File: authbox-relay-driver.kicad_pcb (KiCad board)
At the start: 2 copper layers, 65 x 56 mm, 33 parts, among them J1 GPIO, J2 Screw_Terminal_01x12, Q1 2V7002L, Q2 BC846, Q3 BC846, Q4 2V7002L, U2 MCP1415

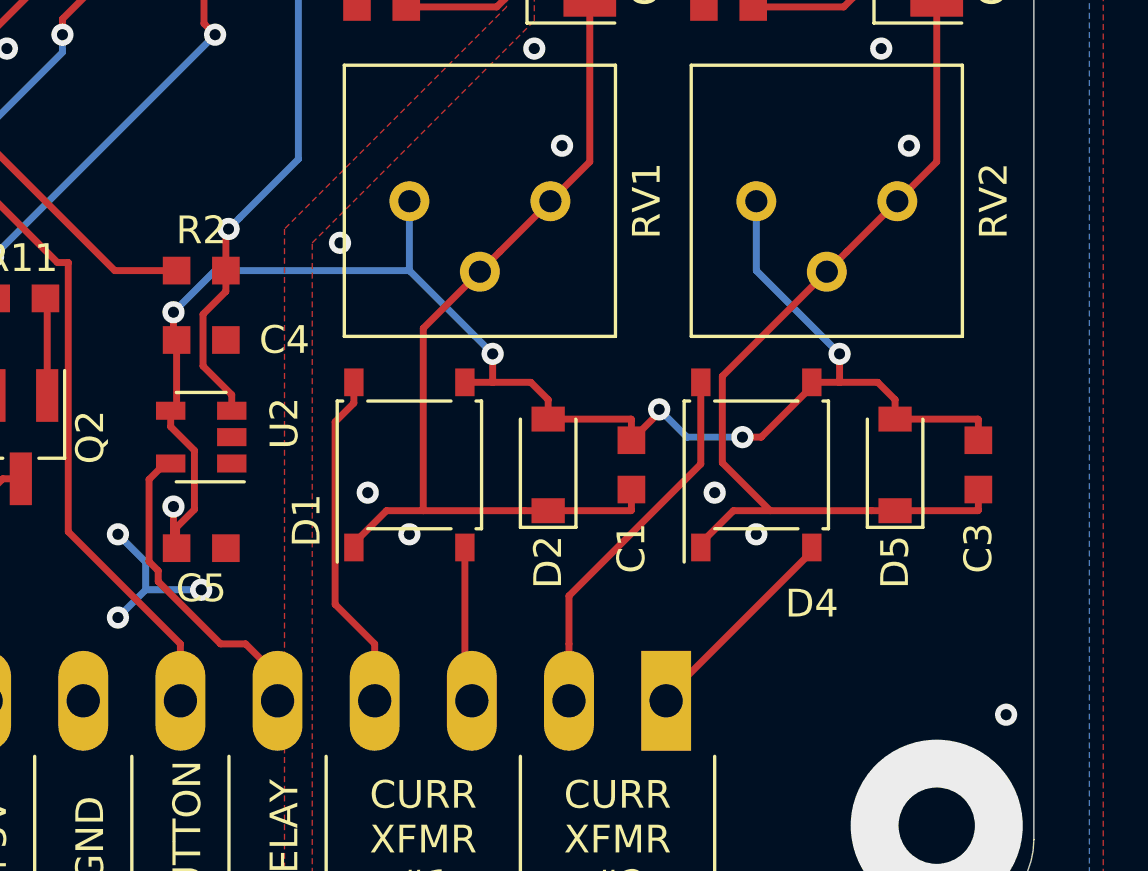
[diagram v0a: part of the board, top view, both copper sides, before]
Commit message: Fixed: * Rectifier bridge footprint. * Pad size for trimmer potentiometers.
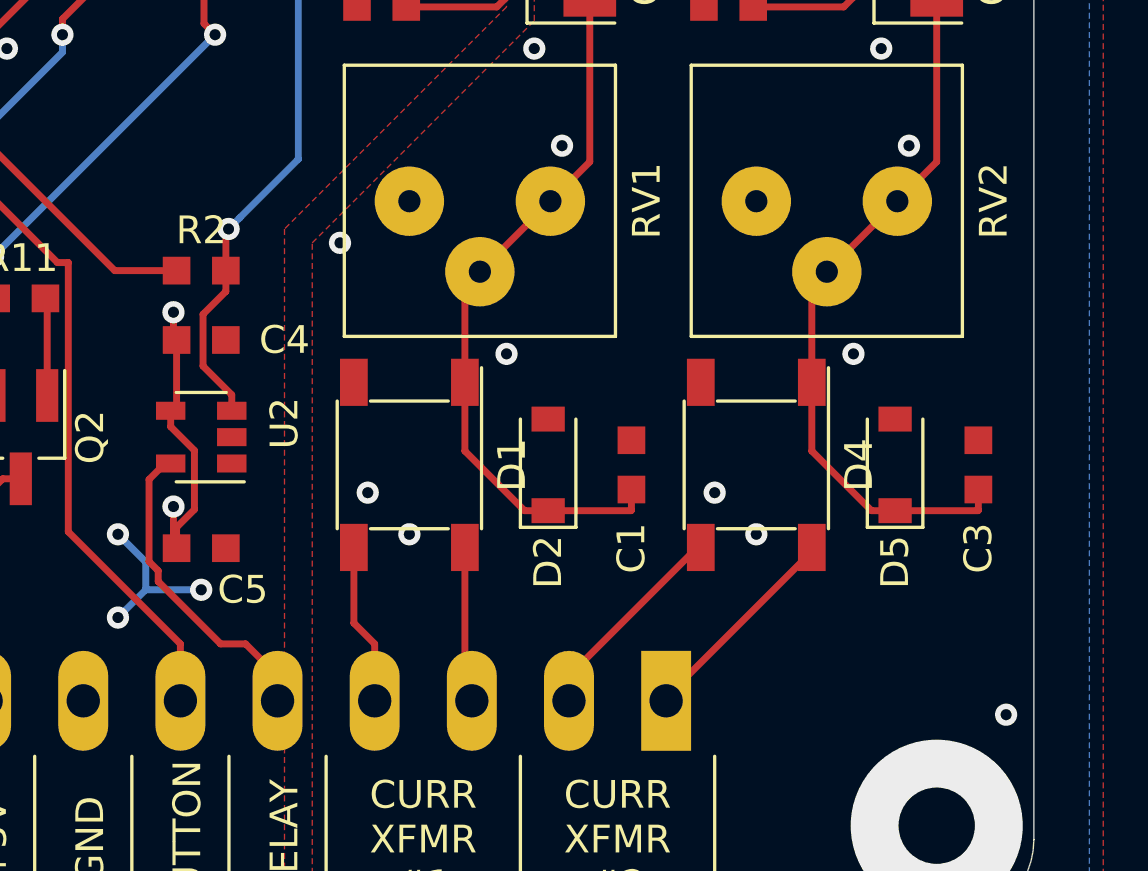
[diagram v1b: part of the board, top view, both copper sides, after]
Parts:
- turned D1 to 270 degrees
- turned D4 to 270 degrees
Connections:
- D1 pad 2: /current-sense/CURR_B -> GND
- D1 pad 3: GND -> /current-sense/CURR_A
- D1 pad 4: /current-sense/CURR_A -> /current-sense/CURR_B
- D4 pad 2: /sheet5C9BD5B1/CURR_B -> GND
- D4 pad 3: GND -> /sheet5C9BD5B1/CURR_A
- D4 pad 4: /sheet5C9BD5B1/CURR_A -> /sheet5C9BD5B1/CURR_B
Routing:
- net GND: track 146.0 -> 97.5 mm, vias 25 -> 23
- net Net-(C3-Pad1): track 33.5 -> 25.6 mm
- net Net-(C1-Pad1): track 32.1 -> 25.6 mm
- net /current-sense/CURR_A: track 12.3 -> 5.84 mm
- net /sheet5C9BD5B1/CURR_A: track 13.4 -> 7.57 mm

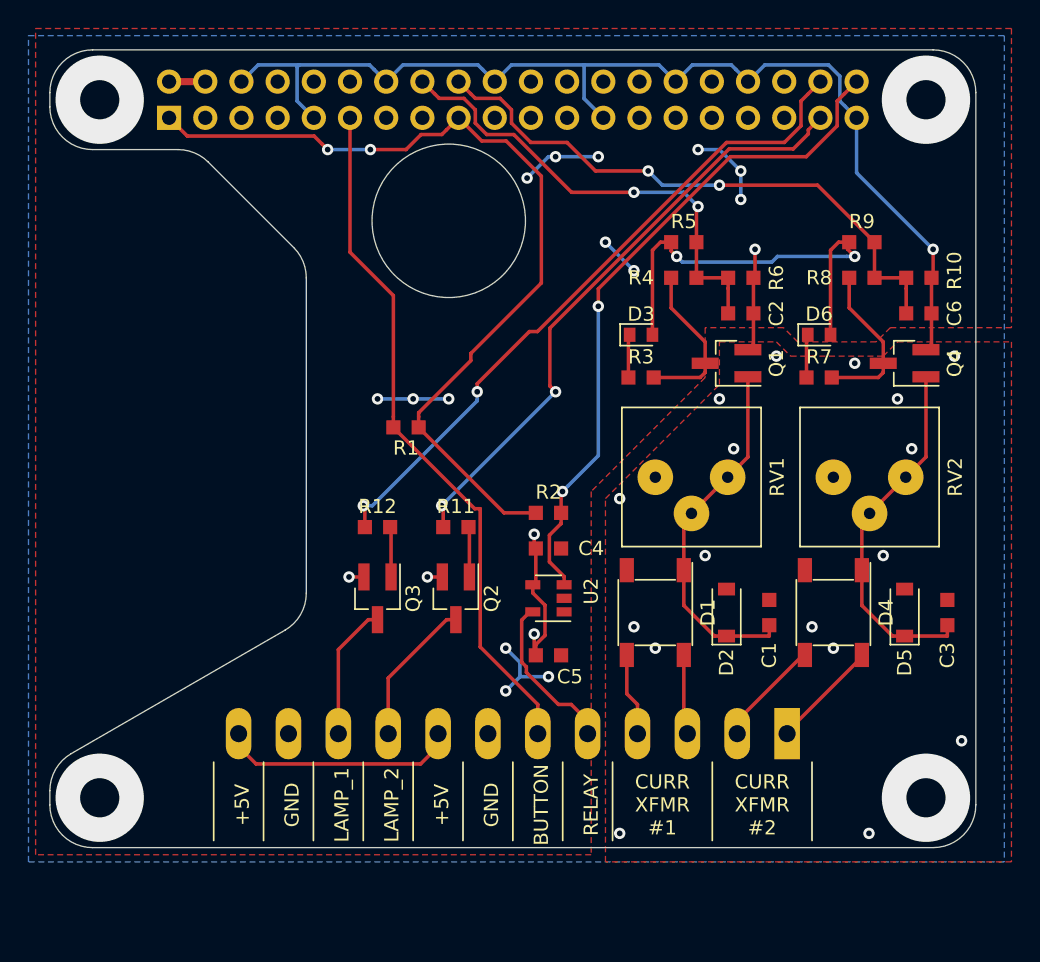
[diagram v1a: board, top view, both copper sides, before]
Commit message: Fixed a few solderability issues. Corrected the footprint for the rectifier bridges (D1 and D4).
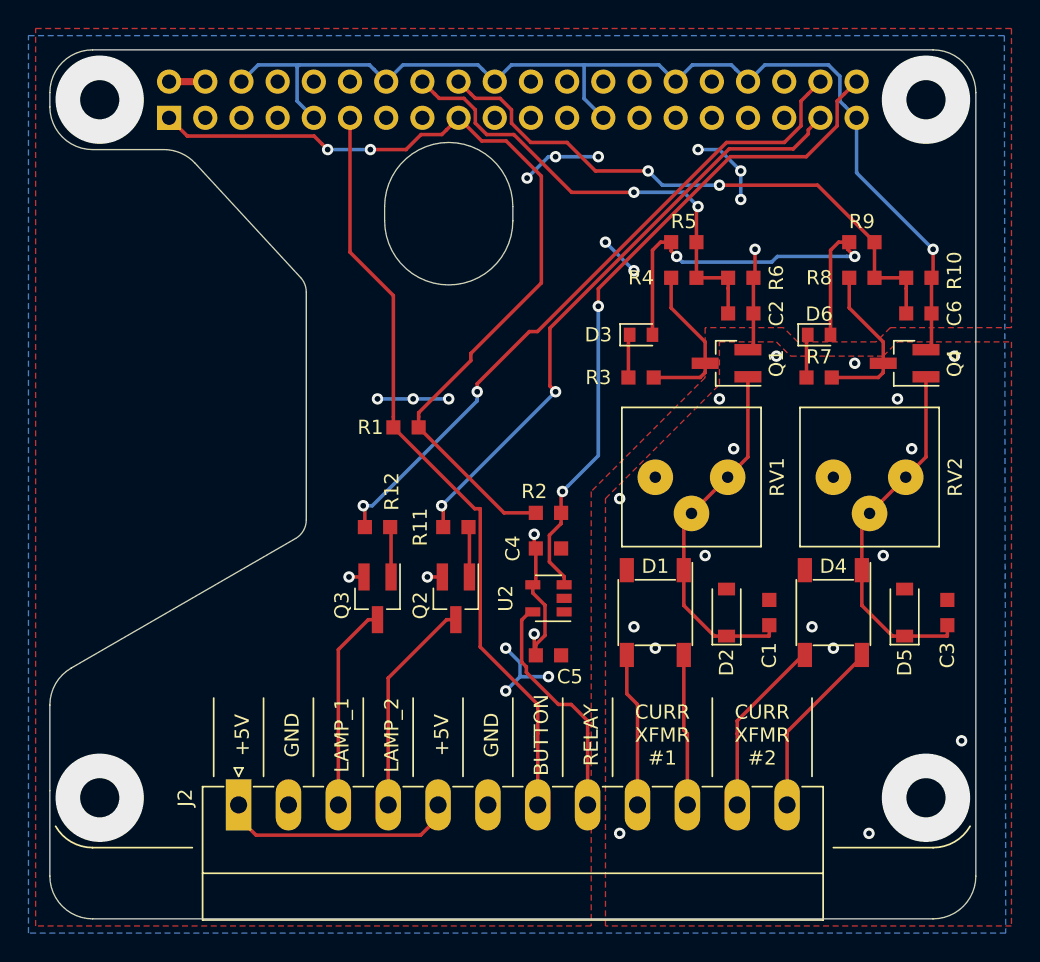
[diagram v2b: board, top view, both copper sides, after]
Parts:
- J2: moved to F.Cu
- moved J2 38.8 mm to (126.8, 139.7), turned to 0 degrees
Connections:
- J2 pad 1: /sheet5C9BD5B1/CURR_B -> +5V
- J2 pad 10: LAMP1 -> /current-sense/CURR_B
- J2 pad 11: GND -> /sheet5C9BD5B1/CURR_A
- J2 pad 12: +5V -> /sheet5C9BD5B1/CURR_B
- J2 pad 2: /sheet5C9BD5B1/CURR_A -> GND
- J2 pad 3: /current-sense/CURR_B -> LAMP1
- J2 pad 4: /current-sense/CURR_A -> LAMP2
- J2 pad 5: Net-(J2-Pad5) -> +5V
- J2 pad 6: B1_LOGIC -> GND
- J2 pad 7: GND -> B1_LOGIC
- J2 pad 8: +5V -> Net-(J2-Pad8)
- J2 pad 9: LAMP2 -> /current-sense/CURR_A
- U2 pad 5: Net-(J2-Pad5) -> Net-(J2-Pad8)
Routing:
- net Net-(J2-Pad8): track 0.00 -> 16.4 mm
- net Net-(J2-Pad5): track 11.4 -> 0.00 mm
- net LAMP2: track 10.3 -> 15.3 mm
- net LAMP1: track 9.52 -> 14.5 mm
- net B1_LOGIC: track 48.9 -> 53.9 mm
- net /current-sense/CURR_A: track 5.84 -> 10.8 mm
- net /sheet5C9BD5B1/CURR_B: track 7.70 -> 12.7 mm
- net /sheet5C9BD5B1/CURR_A: track 7.57 -> 12.6 mm
- net /current-sense/CURR_B: track 5.63 -> 10.6 mm
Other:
- board size 65 x 56 mm -> 65 x 61 mm

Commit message: Replace out of stock 2V7002 with 2N7002. Upgrade to KiCad 7.0.
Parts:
- C1, C3: value C -> 1µF
- C4, C5: value C -> 100nF
- Q1, Q4: value 2V7002L -> 2N7002L
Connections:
- C1 pad 1: Net-(C1-Pad1) -> Net-(D1-+)
- C3 pad 1: Net-(C3-Pad1) -> Net-(D4-+)
- D1 pad 1: Net-(C1-Pad1) -> Net-(D1-+)
- D2 pad 1: Net-(C1-Pad1) -> Net-(D1-+)
- D4 pad 1: Net-(C3-Pad1) -> Net-(D4-+)
- D5 pad 1: Net-(C3-Pad1) -> Net-(D4-+)
- J1 pad 10: Net-(J1-Pad10) -> unconnected-(J1-Pin_10-Pad10)
- J1 pad 12: Net-(J1-Pad12) -> unconnected-(J1-Pin_12-Pad12)
- J1 pad 13: Net-(J1-Pad13) -> unconnected-(J1-Pin_13-Pad13)
- J1 pad 15: Net-(J1-Pad15) -> unconnected-(J1-Pin_15-Pad15)
- J1 pad 19: Net-(J1-Pad19) -> unconnected-(J1-Pin_19-Pad19)
- J1 pad 21: Net-(J1-Pad21) -> unconnected-(J1-Pin_21-Pad21)
- J1 pad 22: Net-(J1-Pad22) -> unconnected-(J1-Pin_22-Pad22)
- J1 pad 23: Net-(J1-Pad23) -> unconnected-(J1-Pin_23-Pad23)
- J1 pad 24: Net-(J1-Pad24) -> unconnected-(J1-Pin_24-Pad24)
- J1 pad 26: Net-(J1-Pad26) -> unconnected-(J1-Pin_26-Pad26)
- J1 pad 27: Net-(J1-Pad27) -> unconnected-(J1-Pin_27-Pad27)
- J1 pad 28: Net-(J1-Pad28) -> unconnected-(J1-Pin_28-Pad28)
- J1 pad 29: Net-(J1-Pad29) -> unconnected-(J1-Pin_29-Pad29)
- J1 pad 3: Net-(J1-Pad3) -> unconnected-(J1-Pin_3-Pad3)
- J1 pad 31: Net-(J1-Pad31) -> unconnected-(J1-Pin_31-Pad31)
- J1 pad 32: Net-(J1-Pad32) -> unconnected-(J1-Pin_32-Pad32)
- J1 pad 33: Net-(J1-Pad33) -> unconnected-(J1-Pin_33-Pad33)
- J1 pad 35: Net-(J1-Pad35) -> unconnected-(J1-Pin_35-Pad35)
- J1 pad 36: Net-(J1-Pad36) -> unconnected-(J1-Pin_36-Pad36)
- J1 pad 5: Net-(J1-Pad5) -> unconnected-(J1-Pin_5-Pad5)
- J1 pad 7: Net-(J1-Pad7) -> unconnected-(J1-Pin_7-Pad7)
- J1 pad 8: Net-(J1-Pad8) -> unconnected-(J1-Pin_8-Pad8)
- Q1 pad 1: Net-(C1-Pad1) -> Net-(D1-+)
- Q4 pad 1: Net-(C3-Pad1) -> Net-(D4-+)
- U2 pad 1: Net-(U2-Pad1) -> unconnected-(U2-NC-Pad1)
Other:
- net class Default removed

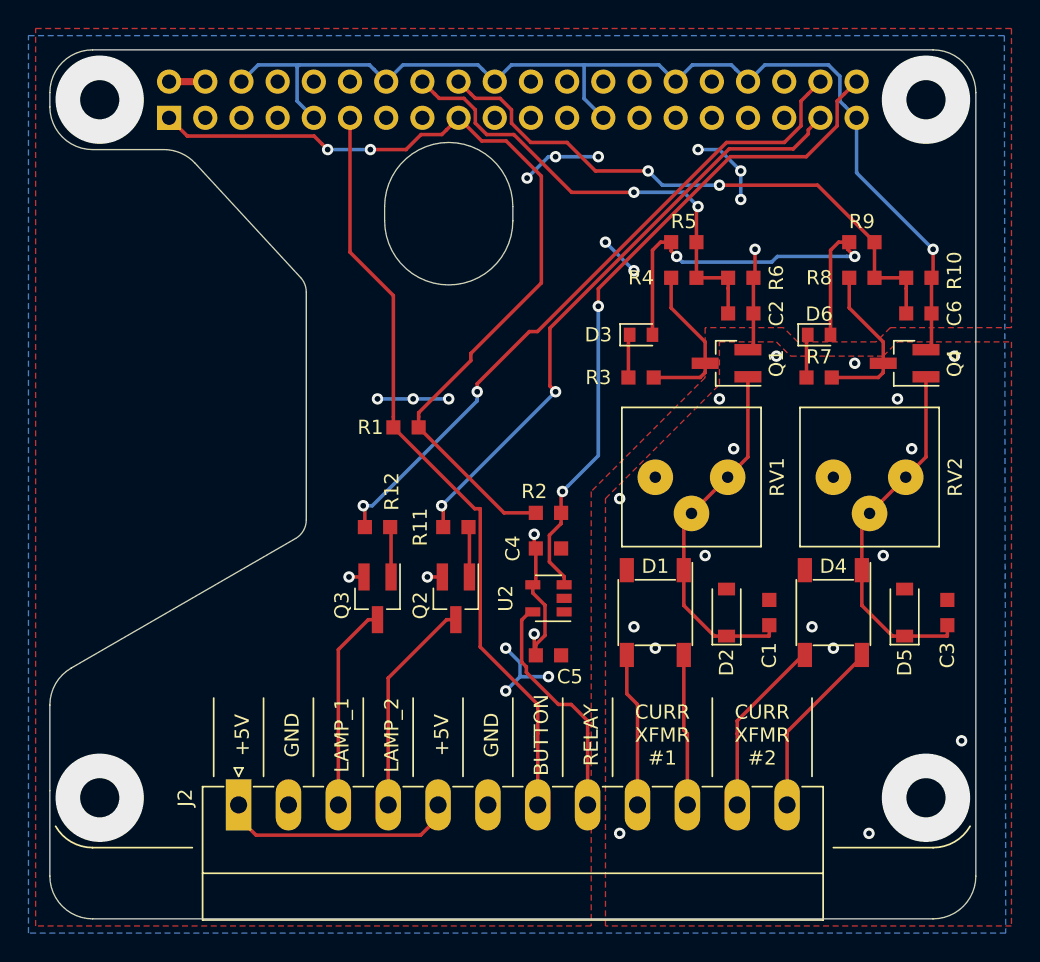
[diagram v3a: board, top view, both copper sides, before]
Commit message: Miscellaneous fixes: * Change to KiCad 8.0. * Modify the cutouts on the board to accomodate a different layout of the   PoE hat (which sits below.) * Transfer the customized footprints into a project-specific "hat-library"   footprints library, rather than leave them with local edits. * Change the mounting holes from through-plated to NPTH.
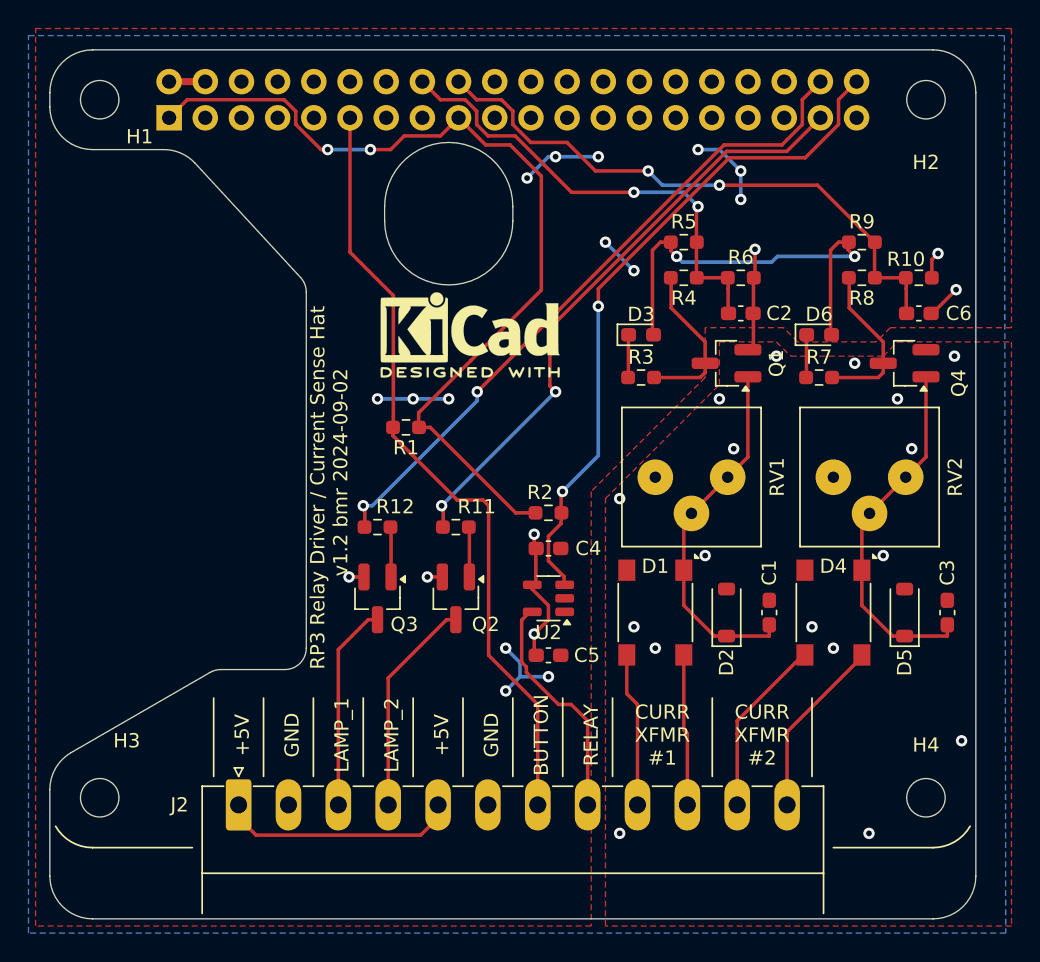
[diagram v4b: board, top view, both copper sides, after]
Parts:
- added H1: MountingHole, MountingHole:MountingHole_2.7mm, F.Cu at (117.0, 90.2)
- added H2: MountingHole, MountingHole:MountingHole_2.7mm, F.Cu at (175.1, 90.2)
- added H3: MountingHole, MountingHole:MountingHole_2.7mm, F.Cu at (117.0, 139.2)
- added H4: MountingHole, MountingHole:MountingHole_2.7mm, F.Cu at (175.1, 139.2)
- added REF**: KiCad-Logo2_5mm_SilkScreen, Symbol:KiCad-Logo2_5mm_SilkScreen, F.Cu at (143.1, 106.7)
- C1, C2, C3, C4, C5, C6: footprint Capacitor_SMD:C_0603_1608Metric_Pad0.99x1.00mm_HandSolder -> Capacitor_SMD:C_0603_1608Metric_Pad1.08x0.95mm_HandSolder
- D1, D4: footprint Diode_SMD:Diode_Bridge_Diotec_ABS -> hat-library:Diode_Bridge_Diotec_ABS
- D3, D6: footprint LED_SMD:LED_0603_1608Metric_Pad0.82x1.00mm_HandSolder -> LED_SMD:LED_0603_1608Metric_Pad1.05x0.95mm_HandSolder
- J1: footprint Connector_PinSocket_2.54mm:PinSocket_2x20_P2.54mm_Vertical -> hat-library:PinSocket_2x20_P2.54mm_Vertical
- J2: footprint Connector_Phoenix_MC:PhoenixContact_MC_1,5_12-G-3.5_1x12_P3.50mm_Horizontal -> hat-library:PhoenixContact_MC_1,5_12-G-3.5_1x12_P3.50mm_Horizontal
- R1, R10, R11, R12, R2, R3, R4, R5, R6, R7, R8, R9: footprint Resistor_SMD:R_0603_1608Metric_Pad0.99x1.00mm_HandSolder -> Resistor_SMD:R_0603_1608Metric_Pad0.98x0.95mm_HandSolder
- RV1, RV2: footprint Potentiometer_THT:Potentiometer_Bourns_3386P_Vertical -> hat-library:Potentiometer_Bourns_3386P_Vertical
- U2: footprint Package_TO_SOT_SMD:SOT-23-5 -> hat-library:SOT-23-5
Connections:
- RV1 pad 2: Net-(C1-Pad1) -> Net-(D1-+)
- RV1 pad 3: Net-(C1-Pad1) -> Net-(D1-+)
- RV2 pad 2: Net-(C3-Pad1) -> Net-(D4-+)
- RV2 pad 3: Net-(C3-Pad1) -> Net-(D4-+)
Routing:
- net GND: track 97.5 -> 23.3 mm, vias 23 -> 24
- net Net-(D4-+): track 0.00 -> 25.6 mm
- net Net-(C3-Pad1): track 25.6 -> 0.00 mm
- net Net-(D1-+): track 0.00 -> 25.6 mm
- net Net-(C1-Pad1): track 25.6 -> 0.00 mm
- net +3V3: track 61.6 -> 63.2 mm
- net B1_LOGIC: track 53.9 -> 54.8 mm
- net (no net): vias 4 -> 0
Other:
- outline, holes or cut-outs redrawn
- rule pad_to_mask_clearance: 0.051 -> 0.02
- rule solder_mask_min_width: 0.25 -> 0.1
- board text added: "RP3 Relay Driver / Current Sense Hat v1.2 bmr 2024-09-02"
